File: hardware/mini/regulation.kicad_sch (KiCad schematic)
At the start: 6 parts, among them U2 AP63203WU

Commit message: mini
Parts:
- removed C22: 100n, Capacitor_SMD:C_0402_1005Metric, symbol Device:C
- removed C23, C25: 22u, Capacitor_SMD:C_0603_1608Metric, symbol Device:C
- removed C24: 10u, Capacitor_SMD:C_1206_3216Metric, symbol Device:C
- removed L2: 3.9uH, Inductor_SMD:L_Changjiang_FNR5020S, symbol Device:L
- removed U2: AP63203WU, Package_TO_SOT_SMD:TSOT-23-6, symbol Regulator_Switching:AP63203WU

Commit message: add interface & RP2040
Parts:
- added C22: 100n, Capacitor_SMD:C_0402_1005Metric, symbol Device:C
- added C23: 10u, Capacitor_SMD:C_1206_3216Metric, symbol Device:C
- added C24, C25: 22u, Capacitor_SMD:C_0603_1608Metric, symbol Device:C
- added L2: 3.9uH, Inductor_SMD:L_Changjiang_FNR5020S, symbol Device:L
- added U2: AP63203WU, Package_TO_SOT_SMD:TSOT-23-6, symbol Regulator_Switching:AP63203WU
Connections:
- new net: C22.1, U2.6 (BST)
- new net: C22.2, L2.1, U2.5 (SW)
- new net +3V3: C24.2, C25.2, L2.2, U2.1 (FB)
- new net GND: C23.2, C24.1, C25.1, U2.4 (GND)
- new net VBUS: C23.1, U2.2 (EN), U2.3 (IN)

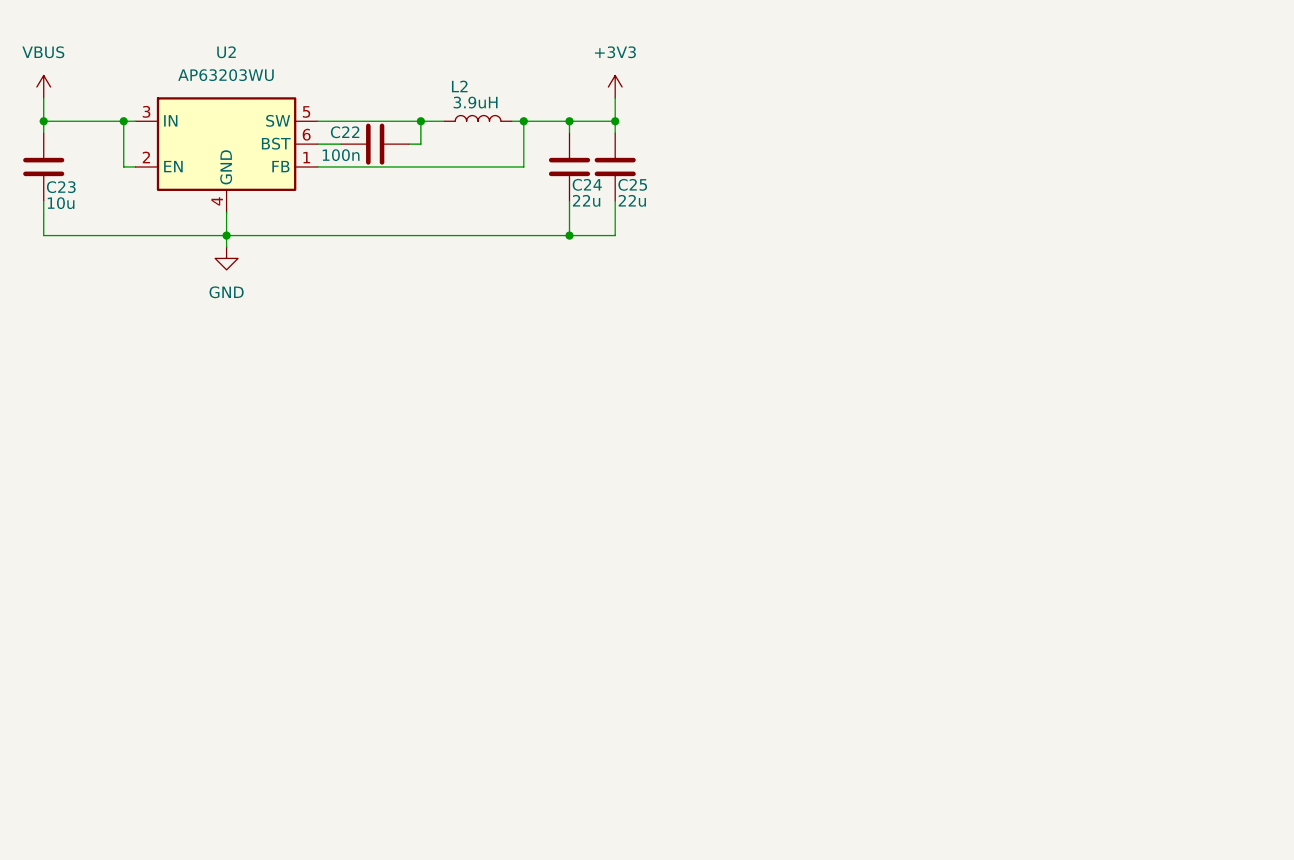
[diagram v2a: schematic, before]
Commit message: finalize parts in schematic
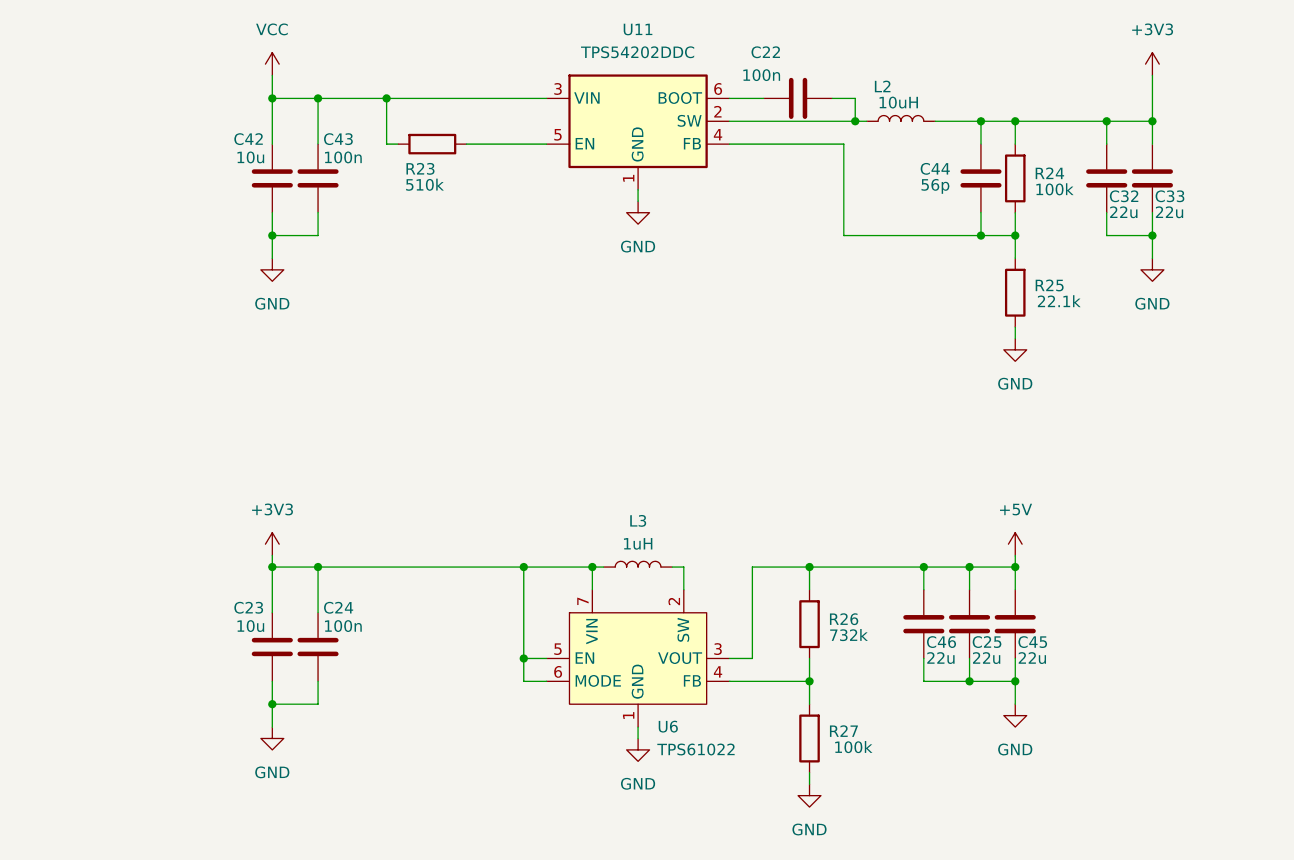
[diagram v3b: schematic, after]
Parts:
- removed U2: AP63203WU, Package_TO_SOT_SMD:TSOT-23-6, symbol Regulator_Switching:AP63203WU
- added C32, C33, C45, C46: 22u, Capacitor_SMD:C_0603_1608Metric, symbol Device:C
- added C42: 10u, Capacitor_SMD:C_1206_3216Metric, symbol Device:C
- added C43: 100n, Capacitor_SMD:C_0402_1005Metric, symbol Device:C
- added C44: 56p, symbol Device:C
- added L3: 1uH, symbol Device:L
- added R23: 510k, symbol Device:R
- added R24, R27: 100k, symbol Device:R
- added R25: 22.1k, symbol Device:R
- added R26: 732k, symbol Device:R
- added U11: TPS54202DDC, Package_TO_SOT_SMD:SOT-23-6, symbol Regulator_Switching:TPS54202DDC
- added U6: TPS61022, Package_DFN_QFN:Texas_RWU0007A_VQFN-7_2x2mm_P0.5mm, symbol Converter_DCDC:TPS61022
- C24: value 22u -> 100n; footprint Capacitor_SMD:C_0603_1608Metric -> Capacitor_SMD:C_0402_1005Metric; LCSC C59461 -> C307331
- L2: value 3.9uH -> 10uH; footprint Inductor_SMD:L_Changjiang_FNR5020S -> Inductor_SMD:L_Changjiang_FXL0530; LCSC C167928 -> C177248
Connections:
- net VBUS is gone; now on net +3V3: C23.1
- net +3V3: now also C32.2, C33.2, C44.2, L3.1, R24.2, U6.5 (EN), U6.6 (MODE), U6.7 (VIN); no longer C25.2
- net GND: now also C32.1, C33.1, C42.2, C43.1, C45.1, C46.1, R25.1, R27.1, U11.1 (GND), U6.1 (GND)
- net at C22.1: now also U11.6 (BOOT)
- net at C22.2, L2.1: now also U11.2 (SW)
- new net: C44.1, R24.1, R25.2, U11.4 (FB)
- new net: L3.2, U6.2 (SW)
- new net: R26.1, R27.2, U6.4 (FB)
- new net: R23.1, U11.5 (EN)
- new net +5V: C25.2, C45.2, C46.2, R26.2, U6.3 (VOUT)
- new net VCC: C42.1, C43.2, R23.2, U11.3 (VIN)
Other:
- moved on the sheet: C22, L2

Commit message: route most
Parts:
- renumbered C42 to C24, C23 to C25, C43 to C26, C24 to C27, C22 to C28, C46 to C29, C25 to C30, C44 to C31, C45 to C32, C32 to C33, C33 to C34, L3 to L2, L2 to L3, R23 to R12, R26 to R13, R27 to R14, R24 to R15, R25 to R16, U11 to U4, U6 to U5

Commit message: ERC run
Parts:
- removed C25: 10u, Capacitor_SMD:C_1206_3216Metric, symbol Device:C
- removed C27: 100n, Capacitor_SMD:C_0402_1005Metric, symbol Device:C
- removed C29, C30, C32: 22u, Capacitor_SMD:C_0603_1608Metric, symbol Device:C
- removed L2: 1uH, symbol Device:L
- removed R13: 732k, symbol Device:R
- removed R14: 100k, symbol Device:R
- removed U5: TPS61022, Package_DFN_QFN:Texas_RWU0007A_VQFN-7_2x2mm_P0.5mm, symbol Converter_DCDC:TPS61022
- renumbered C26 to C25, C28 to C26, C31 to C27, C33 to C28, C34 to C29, L3 to L2, R12 to R11, R15 to R12, R16 to R13
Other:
- moved on the sheet: C24, C25, C26, C27, C28, C29, L2, R11, R12, R13, U4

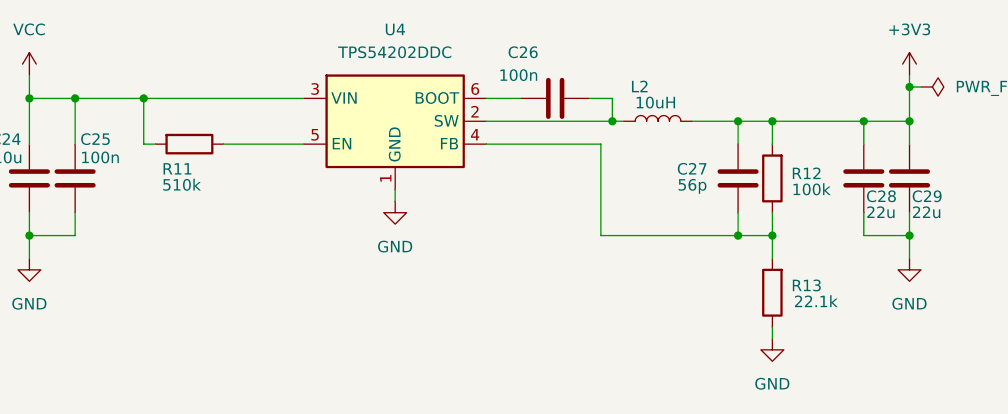
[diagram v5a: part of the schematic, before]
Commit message: assign footprints & LCSC id
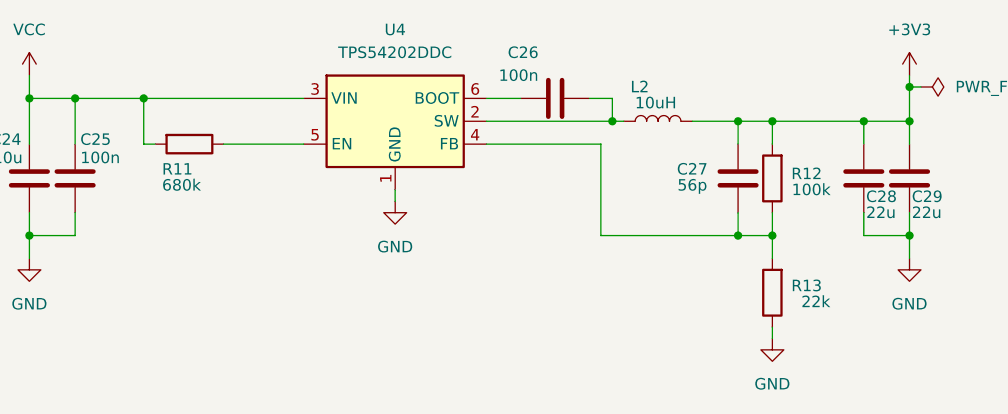
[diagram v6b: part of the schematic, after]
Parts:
- C27: footprint (none) -> Capacitor_SMD:C_0402_1005Metric; LCSC (none) -> C107007
- R11: value 510k -> 680k; footprint (none) -> Resistor_SMD:R_0402_1005Metric; LCSC (none) -> C4131
- R12: footprint (none) -> Resistor_SMD:R_0402_1005Metric; LCSC (none) -> C25741
- R13: value 22.1k -> 22k; footprint (none) -> Resistor_SMD:R_0402_1005Metric; LCSC (none) -> C25768
- U4: LCSC (none) -> C191884
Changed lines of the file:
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@@
 			)
 		)
-		(property "Footprint" ""
+		(property "Footprint" "Resistor_SMD:R_0402_1005Metric"
 			(at 187.198 96.52 90)
 			(effects
@@
 		)
 		(property "Description" "Resistor"
+			(at 185.42 96.52 0)
+			(effects
+				(font
+					(size 1.27 1.27)
+				)
+				(hide yes)
+			)
+		)
+		(property "LCSC" "C25741"
 			(at 185.42 96.52 0)
 			(effects
@@
 			)
 		)
-		(property "Footprint" ""
+		(property "Footprint" "Capacitor_SMD:C_0402_1005Metric"
 			(at 180.6448 92.71 0)
 			(effects
@@
 			)
 		)
+		(property "LCSC" "C107007"
+			(at 181.61 96.52 0)
+			(effects
+				(font
+					(size 1.27 1.27)
+				)
+				(hide yes)
+			)
+		)
 		(pin "1"
 		)
@@
 			)
 		)
-		(property "Value" "22.1k"
+		(property "Value" "22k"
 			(at 190.246 110.236 0)
 			(effects
@@
 			)
 		)
-		(property "Footprint" ""
+		(property "Footprint" "Resistor_SMD:R_0402_1005Metric"
 			(at 187.198 109.22 90)
 			(effects
@@
 		)
 		(property "Description" "Resistor"
+			(at 185.42 109.22 0)
+			(effects
+				(font
+					(size 1.27 1.27)
+				)
+				(hide yes)
+			)
+		)
+		(property "LCSC" "C25768"
 			(at 185.42 109.22 0)
 			(effects
@@
 			)
 		)
-		(property "Value" "510k"
+		(property "Value" "680k"
 			(at 117.602 97.282 90)
 			(effects
@@
 			)
 		)
-		(property "Footprint" ""
+		(property "Footprint" "Resistor_SMD:R_0402_1005Metric"
 			(at 120.65 90.932 90)
 			(effects
@@
 		(property "Description" "Resistor"
 			(at 120.65 92.71 0)
+			(effects
+				(font
+					(size 1.27 1.27)
+				)
+				(hide yes)
+			)
+		)
+		(property "LCSC" "C4131"
+			(at 120.65 92.71 90)
 			(effects
 				(font
@@
 			(at 143.51 90.17 0)
 			(effects
+				(font
+					(size 1.27 1.27)
+				)
+				(hide yes)
+			)
+		)
+		(property "LCSC" "C191884"
+			(at 143.51 90.17 0)
+			(effects

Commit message: finish routing
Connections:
- net VCC renamed VBUS
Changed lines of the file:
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@@
 			)
 		)
-		(property "Value" "VCC"
+		(property "Value" "VBUS"
 			(at 102.87 80.01 0)
 			(effects
@@
 		)
 		(instances
-			(project "mini"
+			(project ""
 				(path "/5aaaac9a-5acd-4aef-ad51-a6d04aa88705/b5f4469e-cca9-4b96-8151-d3c520fcf3a5"
 					(reference "#PWR022")

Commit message: cleanup schematic
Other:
- title: (none) -> Protovolt MINI
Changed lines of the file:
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@@
 	(generator_version "9.0")
 	(paper "A4")
+	(title_block
+		(title "Protovolt MINI")
+		(date "2025-06-16")
+		(rev "A")
+		(comment 3 "MINI")
+		(comment 4 "Protovolt")
+	)
 	(junction
 		(at 200.66 86.36)
